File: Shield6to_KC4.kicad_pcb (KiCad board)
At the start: 2 copper layers, 112.4 x 80 mm, 34 parts, among them J1 DB9, P1 CONN_9, P2 CONN_8, P3 CONN_9, P4 CONN_8, P5 CONN_8, P8 CONN_8, SW1 BOOT, SW2 SW_PUSH, SW3 SW_PUSH, SW4 SW_PUSH, SW5 RESET, U1 ID-12LA, U2 MAX232

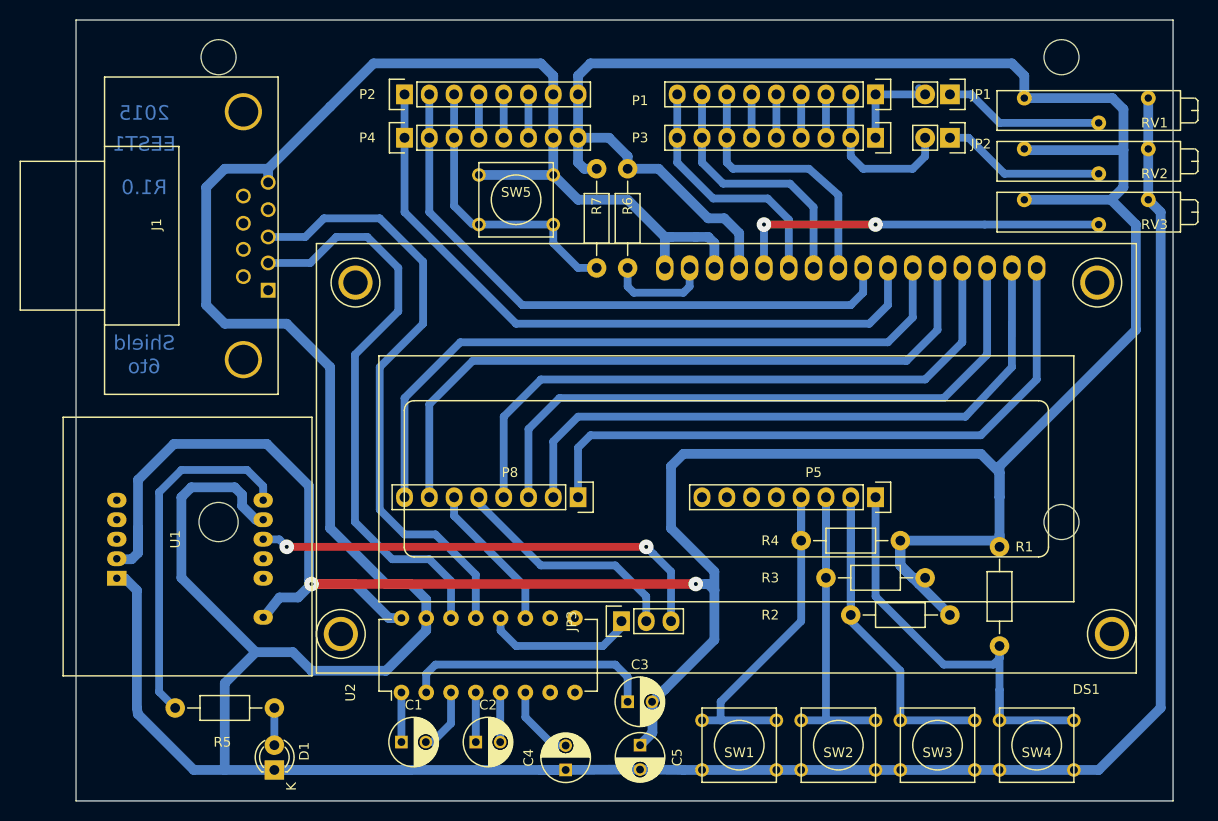
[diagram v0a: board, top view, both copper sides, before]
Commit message: Committer: Esteban Lemos <esteban@mobile.lemos>
 On branch master
 Your branch is up-to-date with 'origin/master'.

 Changes to be committed:
	deleted:    Shield6to.kicad_pcb_sin_micro_1.kicad_pcb-bak
	deleted:    Shield6to.kicad_pcb_sin_micro_1.pro
	deleted:    Shield6to.pro
	modified:   Shield6to_KC4.bak
	renamed:    Shield6to_KC4_Con_RFID.kicad_pcb -> Shield6to_KC4.kicad_pcb
	deleted:    Shield6to_KC4.kicad_pcb-bak
	modified:   Shield6to_KC4.net
	modified:   Shield6to_KC4.pro
	modified:   Shield6to_KC4.sch
	deleted:    Shield6to_KC4_Con_RFID.kicad_pcb-bak
	deleted:    Shield6to_KC4_Con_RFID.pro
	deleted:    Shield6to_KC4_SinRFID.pro
	deleted:    Shield6to_KC4_sin_conectores.kicad_pcb-bak
	deleted:    Shield6to_KC4_sin_conectores.pro
	deleted:    _autosave-Shield6to_KC4.kicad_pcb
	deleted:    _autosave-Shield6to_KC4_sin_conectores.kicad_pcb
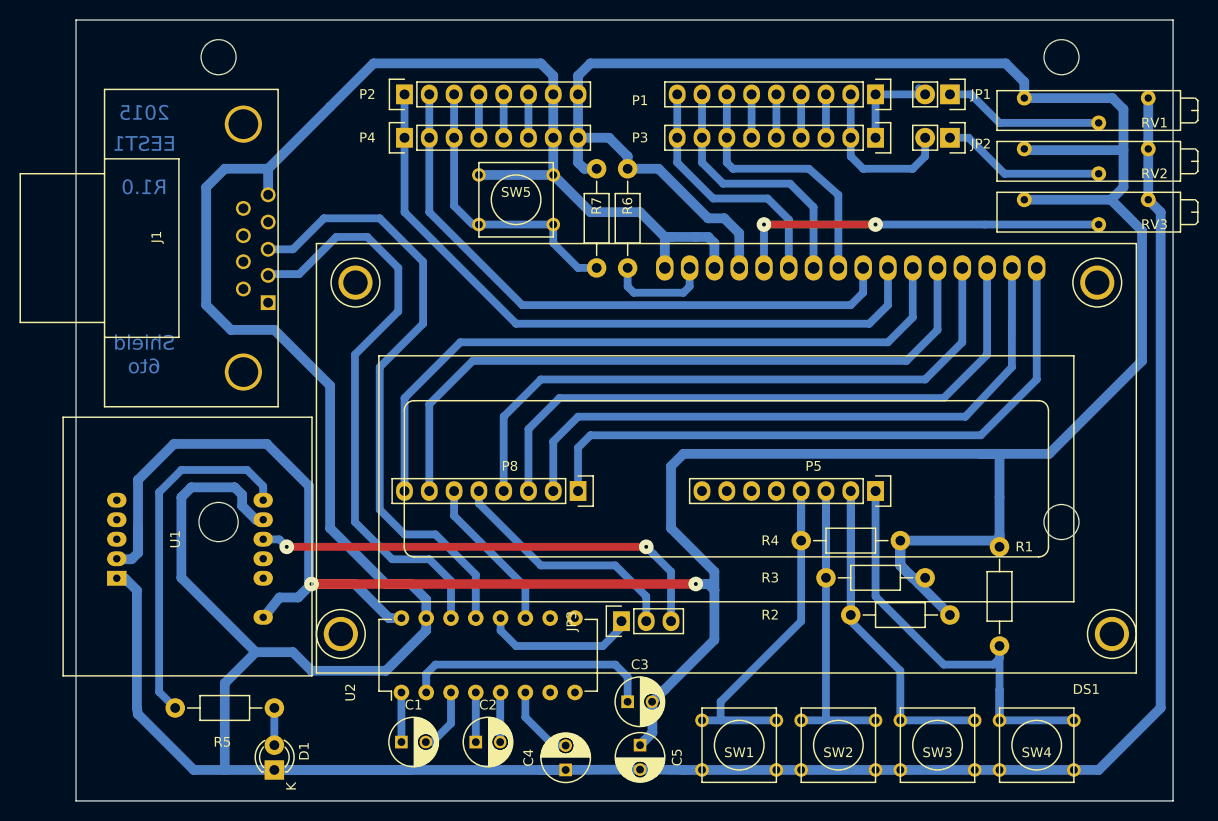
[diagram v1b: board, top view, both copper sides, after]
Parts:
- SW4: value SW_PUSH -> BOT
- moved J1 1.27 mm to (73.7, 76.8)
- moved P5 0.64 mm to (137.2, 101.6)
- moved P8 0.64 mm to (106.7, 101.6)
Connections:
- net Net-(DS1-Pad15) renamed /LED+
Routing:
- net +5V: track 368.1 -> 369.8 mm
- net /RB6: track 44.6 -> 45.9 mm
- net /RB5: track 38.7 -> 40.0 mm
- net /RB4: track 38.3 -> 39.6 mm
- net TX: track 15.4 -> 16.0 mm
- net RX: track 24.3 -> 24.9 mm
- net /RD7: track 66.4 -> 65.8 mm
- net /RD5: track 66.0 -> 65.4 mm
- net /RD4: track 66.0 -> 65.4 mm
- net /RD3: track 71.1 -> 70.5 mm
- net /RD2: track 70.7 -> 70.1 mm
- net /RB7: track 45.7 -> 46.3 mm
- net /RD6: track 66.1 -> 65.5 mm
- net Net-(J1-Pad3): track 62.8 -> 63.3 mm
- net Net-(J1-Pad2): track 59.8 -> 60.3 mm
